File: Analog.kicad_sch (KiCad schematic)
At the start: 18 parts, among them U5 LM741, U6 LM741

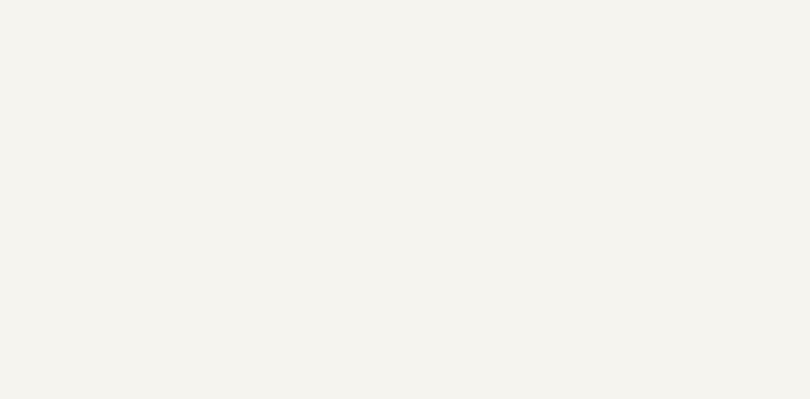
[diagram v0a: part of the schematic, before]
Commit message: added a pinheader for analog signal in
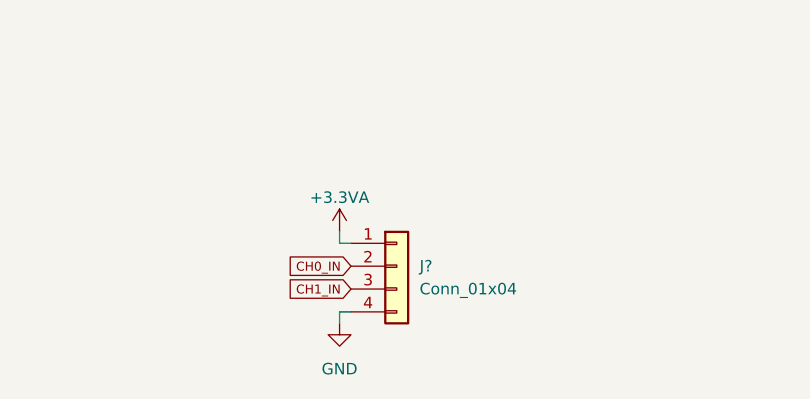
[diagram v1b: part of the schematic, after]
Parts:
- added J?: Conn_01x04, Connector_PinHeader_2.54mm:PinHeader_1x04_P2.54mm_Vertical, symbol Connector_Generic:Conn_01x04
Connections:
- net +3.3VA: now also J?.1 (Pin_1)
- net CH0_IN: now also J?.2 (Pin_2)
- net CH1_IN: now also J?.3 (Pin_3)
- net GND: now also J?.4 (Pin_4)
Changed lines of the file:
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@@
+    (stroke (width 0) (type default) (color 0 0 0 0))
+  )
+  (wire (pts (xy 110.49 151.13) (xy 110.49 149.86))
     (stroke (width 0) (type default) (color 0 0 0 0))
   )
@@
     (stroke (width 0) (type default) (color 0 0 0 0))
   )
+  (wire (pts (xy 110.49 140.97) (xy 110.49 142.24))
+    (stroke (width 0) (type default) (color 0 0 0 0))
+  )
   (wire (pts (xy 194.31 78.74) (xy 194.31 82.55))
     (stroke (width 0) (type default) (color 0 0 0 0))
@@
     (stroke (width 0) (type default) (color 0 0 0 0))
   )
+  (wire (pts (xy 110.49 149.86) (xy 111.76 149.86))
+    (stroke (width 0) (type default) (color 0 0 0 0))
+  )
   (wire (pts (xy 69.85 85.09) (xy 74.93 85.09))
     (stroke (width 0) (type default) (color 0 0 0 0))
@@
   )
   (wire (pts (xy 46.99 85.09) (xy 48.26 85.09))
+    (stroke (width 0) (type default) (color 0 0 0 0))
+  )
+  (wire (pts (xy 110.49 142.24) (xy 111.76 142.24))
     (stroke (width 0) (type default) (color 0 0 0 0))
   )
@@
   (label "CH0_+" (at 71.12 85.09 0)
     (effects (font (size 0.5 0.5)) (justify left bottom))
+  )
+  (global_label "CH0_IN" (shape input) (at 111.76 144.78 180) (fields_autoplaced)
+    (effects (font (size 1 1)) (justify right))
+    (property "Intersheet References" "${INTERSHEET_REFS}" (id 0) (at 104.5743 144.7175 0)
+      (effects (font (size 1 1)) (justify right) hide)
+    )
+  )
+  (global_label "CH1_IN" (shape input) (at 111.76 147.32 180) (fields_autoplaced)
+    (effects (font (size 1 1)) (justify right))
+    (property "Intersheet References" "${INTERSHEET_REFS}" (id 0) (at 104.5743 147.2575 0)
+      (effects (font (size 1 1)) (justify right) hide)
+    )
   )
   (global_label "ADC_CH1_IN" (shape input) (at 224.79 90.17 0) (fields_autoplaced)
@@
     (pin "2")
   )
+  (symbol (lib_id "Connector_Generic:Conn_01x04") (at 116.84 144.78 0) (unit 1)
+    (in_bom yes) (on_board yes) (fields_autoplaced)
+    (property "Reference" "J?" (id 0) (at 119.38 144.7799 0)
+      (effects (font (size 1.27 1.27)) (justify left))
+    )
+    (property "Value" "Conn_01x04" (id 1) (at 119.38 147.3199 0)
+      (effects (font (size 1.27 1.27)) (justify left))
+    )
+    (property "Footprint" "Connector_PinHeader_2.54mm:PinHeader_1x04_P2.54mm_Vertical" (id 2) (at 116.84 144.78 0)
+      (effects (font (size 1.27 1.27)) hide)
+    )
+    (property "Datasheet" "~" (id 3) (at 116.84 144.78 0)
+      (effects (font (size 1.27 1.27)) hide)
+    )
+    (pin "1")
+    (pin "2")
+    (pin "3")
+    (pin "4")
+  )
   (symbol (lib_id "Device:C_Small") (at 54.61 88.9 180) (unit 1)
     (in_bom yes) (on_board yes)
@@
     (pin "1")
   )
+  (symbol (lib_id "power:GND") (at 110.49 151.13 0) (unit 1)
+    (in_bom yes) (on_board yes) (fields_autoplaced)
+    (property "Reference" "#PWR?" (id 0) (at 110.49 157.48 0)
+      (effects (font (size 1.27 1.27)) hide)
+    )
+    (property "Value" "GND" (id 1) (at 110.49 156.21 0))
+    (property "Footprint" "" (id 2) (at 110.49 151.13 0)
+      (effects (font (size 1.27 1.27)) hide)
+    )
+    (property "Datasheet" "" (id 3) (at 110.49 151.13 0)
+      (effects (font (size 1.27 1.27)) hide)
+    )
+    (pin "1")
+  )
   (symbol (lib_id "power:GND") (at 107.95 100.33 0) (unit 1)
     (in_bom yes) (on_board yes)
@@
       (effects (font (size 1.27 1.27)) hide)
     )
+    (pin "1")
+  )
+  (symbol (lib_id "power:+3.3VA") (at 110.49 140.97 0) (unit 1)
+    (in_bom yes) (on_board yes)
+    (property "Reference" "#PWR?" (id 0) (at 110.49 144.78 0)
+      (effects (font (size 1.27 1.27)) hide)
+    )
+    (property "Value" "+3.3VA" (id 1) (at 110.49 137.16 0))
+    (property "Footprint" "" (id 2) (at 110.49 140.97 0)
+      (effects (font (size 1.27 1.27)) hide)
+    )
+    (property "Datasheet" "" (id 3) (at 110.49 140.97 0)
+      (effects (font (size 1.27 1.27)) hide)
+    )

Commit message: Added polygons
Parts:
- gave numbers to parts that had none: 1
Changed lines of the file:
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@@
   (symbol (lib_id "Connector_Generic:Conn_01x04") (at 116.84 144.78 0) (unit 1)
     (in_bom yes) (on_board yes) (fields_autoplaced)
-    (property "Reference" "J?" (id 0) (at 119.38 144.7799 0)
+    (property "Reference" "J6" (id 0) (at 119.38 144.7799 0)
       (effects (font (size 1.27 1.27)) (justify left))
     )
@@
   (symbol (lib_id "power:GND") (at 110.49 151.13 0) (unit 1)
     (in_bom yes) (on_board yes) (fields_autoplaced)
-    (property "Reference" "#PWR?" (id 0) (at 110.49 157.48 0)
+    (property "Reference" "#PWR0165" (id 0) (at 110.49 157.48 0)
       (effects (font (size 1.27 1.27)) hide)
     )
@@
   (symbol (lib_id "power:+3.3VA") (at 110.49 140.97 0) (unit 1)
     (in_bom yes) (on_board yes)
-    (property "Reference" "#PWR?" (id 0) (at 110.49 144.78 0)
+    (property "Reference" "#PWR0167" (id 0) (at 110.49 144.78 0)
       (effects (font (size 1.27 1.27)) hide)
     )

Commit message: added some relevant datasheets
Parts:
- U5, U6: value LM741 -> (none); footprint Package_SO:SOIC-8_3.9x4.9mm_P1.27mm -> (none)
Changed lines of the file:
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@@
     (in_bom yes) (on_board yes)
     (property "Reference" "U6" (id 0) (at 85.09 91.44 0))
-    (property "Value" "LM741" (id 1) (at 85.09 93.98 0))
-    (property "Footprint" "Package_SO:SOIC-8_3.9x4.9mm_P1.27mm" (id 2) (at 83.82 86.36 0)
+    (property "Value" "" (id 1) (at 85.09 93.98 0))
+    (property "Footprint" "" (id 2) (at 83.82 86.36 0)
       (effects (font (size 1.27 1.27)) hide)
     )
@@
     (in_bom yes) (on_board yes)
     (property "Reference" "U5" (id 0) (at 199.39 93.98 0))
-    (property "Value" "LM741" (id 1) (at 199.39 96.52 0))
-    (property "Footprint" "Package_SO:SOIC-8_3.9x4.9mm_P1.27mm" (id 2) (at 198.12 88.9 0)
-      (effects (font (size 1.27 1.27)) hide)
-    )
+    (property "Value" "" (id 1) (at 199.39 96.52 0))
+    (property "Footprint" "" (id 2) (at 198.12 88.9 0)
+      (effects (font (size 1.27 1.27)) hide)
+    )

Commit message: changed footprint of caps
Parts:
- U5, U6: value (none) -> UA741; footprint (none) -> Package_SO:SOIC-8_3.9x4.9mm_P1.27mm
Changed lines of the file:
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@@
     (in_bom yes) (on_board yes)
     (property "Reference" "U6" (id 0) (at 85.09 91.44 0))
-    (property "Value" "" (id 1) (at 85.09 93.98 0))
-    (property "Footprint" "" (id 2) (at 83.82 86.36 0)
+    (property "Value" "UA741" (id 1) (at 85.09 93.98 0))
+    (property "Footprint" "Package_SO:SOIC-8_3.9x4.9mm_P1.27mm" (id 2) (at 83.82 86.36 0)
       (effects (font (size 1.27 1.27)) hide)
     )
@@
     (in_bom yes) (on_board yes)
     (property "Reference" "U5" (id 0) (at 199.39 93.98 0))
-    (property "Value" "" (id 1) (at 199.39 96.52 0))
-    (property "Footprint" "" (id 2) (at 198.12 88.9 0)
-      (effects (font (size 1.27 1.27)) hide)
-    )
+    (property "Value" "UA741" (id 1) (at 199.39 96.52 0))
+    (property "Footprint" "Package_SO:SOIC-8_3.9x4.9mm_P1.27mm" (id 2) (at 198.12 88.9 0)
+      (effects (font (size 1.27 1.27)) hide)
+    )

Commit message: grounded mounting holes gnd top layer polygon and cool looking gnd strips on analog side
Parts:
- D3, D4, D5, D6: value D_Zener -> 3V6
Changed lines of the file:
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@@
       (effects (font (size 1.27 1.27)) (justify left))
     )
-    (property "Value" "D_Zener" (id 1) (at 212.09 83.82 90)
+    (property "Value" "3V6" (id 1) (at 215.9 83.82 90)
       (effects (font (size 1.27 1.27)) (justify left))
     )
@@
       (effects (font (size 1.27 1.27)) (justify left))
     )
-    (property "Value" "D_Zener" (id 1) (at 224.79 99.06 90)
+    (property "Value" "3V6" (id 1) (at 224.79 99.06 90)
       (effects (font (size 1.27 1.27)) (justify left))
     )
@@
   (symbol (lib_id "Device:D_Zener") (at 107.95 80.01 270) (unit 1)
     (in_bom yes) (on_board yes)
-    (property "Reference" "D4" (id 0) (at 102.87 78.74 90)
-      (effects (font (size 1.27 1.27)) (justify left))
-    )
-    (property "Value" "D_Zener" (id 1) (at 97.79 81.28 90)
+    (property "Reference" "D4" (id 0) (at 110.49 78.74 90)
+      (effects (font (size 1.27 1.27)) (justify left))
+    )
+    (property "Value" "3V6" (id 1) (at 110.49 81.28 90)
       (effects (font (size 1.27 1.27)) (justify left))
     )
@@
       (effects (font (size 1.27 1.27)) (justify left))
     )
-    (property "Value" "D_Zener" (id 1) (at 110.49 96.52 90)
-      (effects (font (size 1.27 1.27)) (justify left))
-    )
+    (property "Value" "3V6" (id 1) (at 110.49 96.52 90)
+      (effects (font (size 1.27 1.27)) (justify left))
+    )

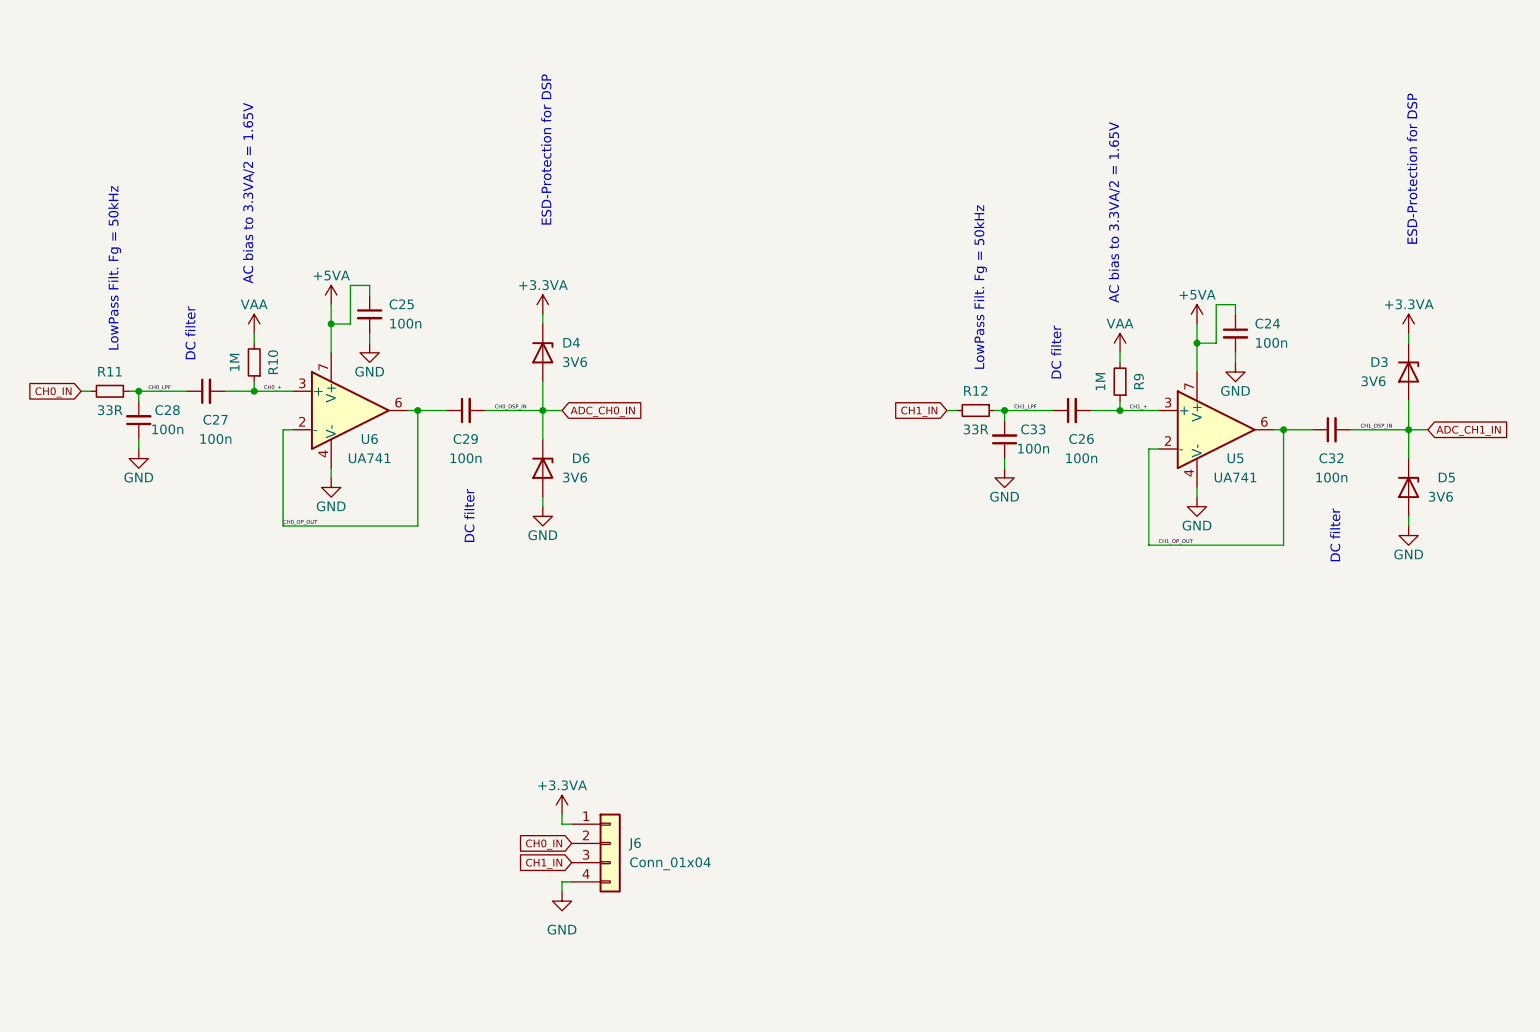
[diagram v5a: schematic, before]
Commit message: replaced 741 opamp for lm358 due to cost reasons
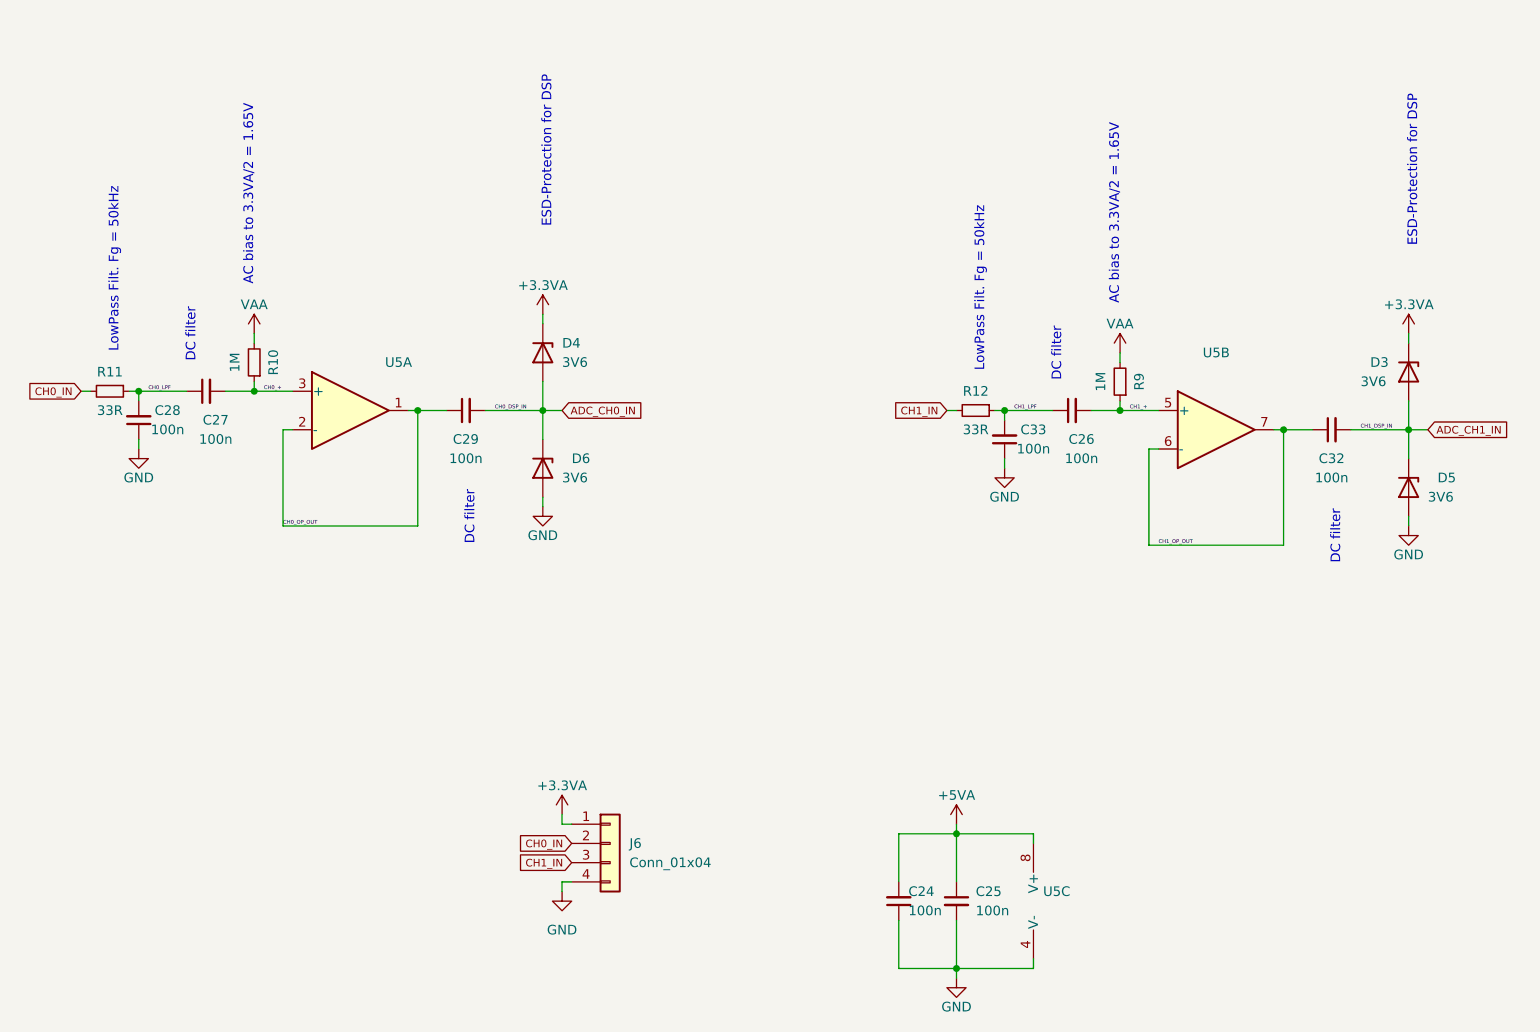
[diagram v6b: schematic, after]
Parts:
- removed U5, U6: UA741, Package_SO:SOIC-8_3.9x4.9mm_P1.27mm, symbol Amplifier_Operational:LM741
- added U5: (no value), symbol Amplifier_Operational:LM358
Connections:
- net +5VA: now also C24.2, U5.8 (V+); no longer C24.1
- net CH0_+: now also U5.3 (+)
- net CH0_OP_OUT: now also U5.1, U5.2 (-)
- net CH1_+: now also U5.5 (+)
- net CH1_OP_OUT: now also U5.6 (-), U5.7
- net GND: now also C24.1, U5.4 (V-); no longer C24.2
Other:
- moved on the sheet: C25

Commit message: finished
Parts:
- U5: value (none) -> LM358; footprint (none) -> Package_SO:SOIC-8_3.9x4.9mm_P1.27mm
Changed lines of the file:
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@@
     (in_bom yes) (on_board yes) (fields_autoplaced)
     (property "Reference" "U5" (id 0) (at 196.85 80.01 0))
-    (property "Value" "" (id 1) (at 196.85 82.55 0))
-    (property "Footprint" "" (id 2) (at 196.85 90.17 0)
+    (property "Value" "LM358" (id 1) (at 196.85 82.55 0))
+    (property "Footprint" "Package_SO:SOIC-8_3.9x4.9mm_P1.27mm" (id 2) (at 196.85 90.17 0)
       (effects (font (size 1.27 1.27)) hide)
     )
@@
       (effects (font (size 1.27 1.27)) (justify left))
     )
-    (property "Value" "" (id 1) (at 173.99 153.6699 0)
+    (property "Value" "LM358" (id 1) (at 173.99 153.6699 0)
       (effects (font (size 1.27 1.27)) (justify left))
     )
-    (property "Footprint" "" (id 2) (at 175.26 152.4 0)
+    (property "Footprint" "Package_SO:SOIC-8_3.9x4.9mm_P1.27mm" (id 2) (at 175.26 152.4 0)
       (effects (font (size 1.27 1.27)) hide)
     )
@@
     (in_bom yes) (on_board yes)
     (property "Reference" "U5" (id 0) (at 88.9 81.28 0))
-    (property "Value" "" (id 1) (at 90.17 83.82 0))
-    (property "Footprint" "" (id 2) (at 82.55 87.63 0)
+    (property "Value" "LM358" (id 1) (at 90.17 83.82 0))
+    (property "Footprint" "Package_SO:SOIC-8_3.9x4.9mm_P1.27mm" (id 2) (at 82.55 87.63 0)
       (effects (font (size 1.27 1.27)) hide)
     )
